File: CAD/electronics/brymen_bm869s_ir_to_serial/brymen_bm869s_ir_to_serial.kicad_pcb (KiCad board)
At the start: 2 copper layers, 42.5 x 13.5 mm, 8 parts, among them J1 Conn_01x04_Male, Q1 2N3904, U1 ATtiny84A-PU

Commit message: changes...?
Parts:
- Q1: value 2N3904 -> BC817; footprint Package_TO_SOT_SMD:SOT-23 -> TO_SOT_Packages_SMD:SOT-23
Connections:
- Q1 pad 1: GND -> Net-(Q1-Pad1)
- Q1 pad 2: Net-(Q1-Pad2) -> GND
- R3 pad 1: Net-(Q1-Pad2) -> Net-(Q1-Pad1)
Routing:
- net Net-(Q1-Pad1): track 0.00 -> 6.30 mm
- net Net-(Q1-Pad2): track 5.45 -> 0.00 mm
- net GND: vias 1 -> 0

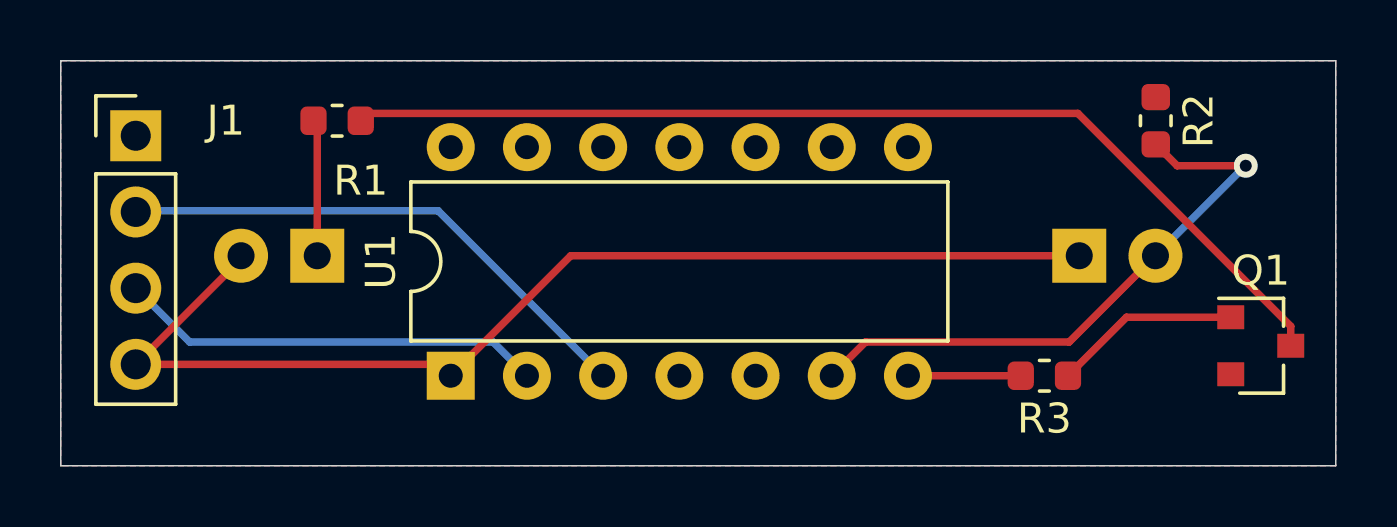
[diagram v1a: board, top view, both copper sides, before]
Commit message: Wrong distance between the IR-diodes, would not fit in the enclosure.
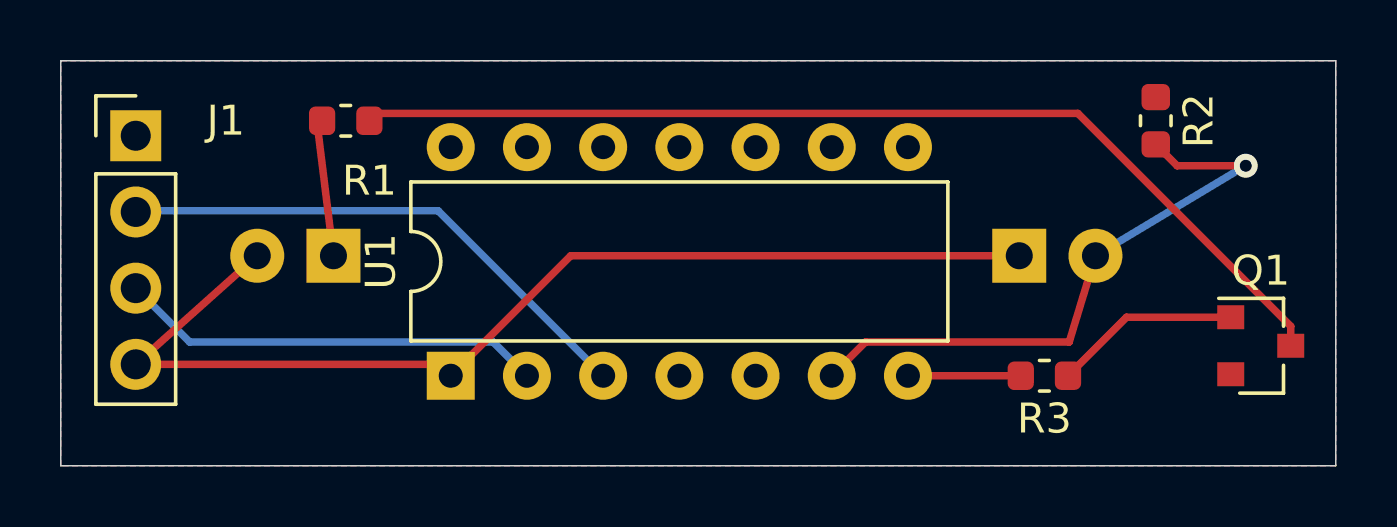
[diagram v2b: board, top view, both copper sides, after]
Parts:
- moved D2 2.00 mm to (82.0, 67.5)
- moved D1 0.54 mm to (59.1, 67.5)
- moved R1 0.29 mm to (59.5, 63.0)
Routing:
- net +5V: track 38.3 -> 37.2 mm
- net /M-RX: track 20.0 -> 20.5 mm
